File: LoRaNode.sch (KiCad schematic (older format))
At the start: 31 parts, among them J1 Conn_01x09, J2 Conn_01x03, J4 ISP, J5 Conn_01x06, J8 D2, J9 D3, SW1 SW_Push, U1 RFM95W-868S2, U4 ATMEGA328P-AU, Y1 8MHz HC5032/4

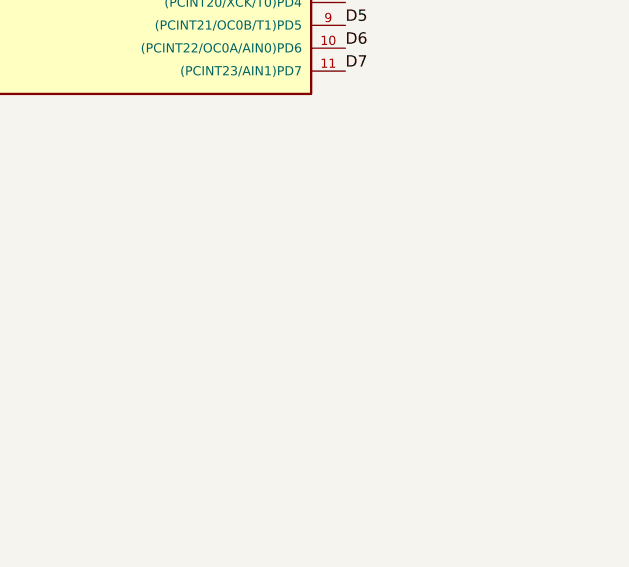
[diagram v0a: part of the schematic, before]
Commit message: Added mounting holes
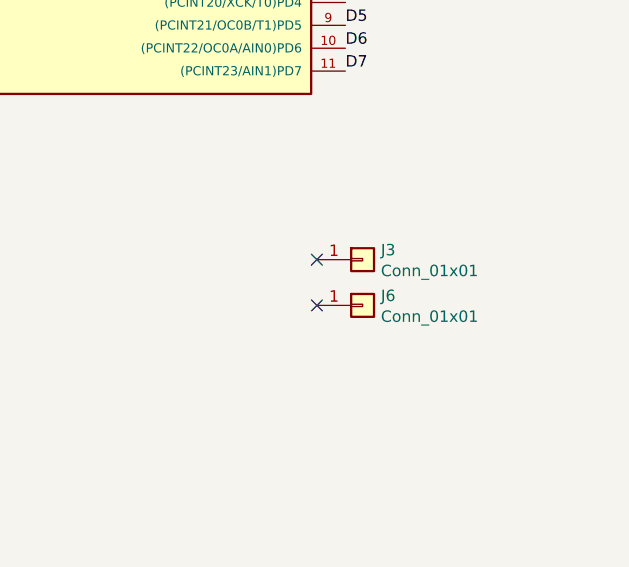
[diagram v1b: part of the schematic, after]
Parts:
- added J3, J6: Conn_01x01, MountingHole:MountingHole_2.2mm_M2, symbol Connector:Conn_01x01
- U1: footprint riske:HOPERF_RFM95W_SMD -> MYLIB:HOPERF_RFM95W_SMD
- U4: footprint Housings_QFP:TQFP-32_7x7mm_Pitch0.8mm -> Package_QFP:TQFP-32_7x7mm_P0.8mm
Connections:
- no-connect marks 3 -> 5
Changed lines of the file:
@@
 F 0 "U1" H 3275 3378 50  0000 C CNN
 F 1 "RFM95W-868S2" H 3625 3150 50  0000 C CNN
-F 2 "riske:HOPERF_RFM95W_SMD" H -25 4350 50  0001 C CNN
+F 2 "MYLIB:HOPERF_RFM95W_SMD" H -25 4350 50  0001 C CNN
 F 3 "" H -25 4350 50  0001 C CNN
 	1    3275 2700
@@
 F 0 "U4" H 7475 4867 50  0000 C CNN
 F 1 "ATMEGA328P-AU" H 7475 4776 50  0000 C CNN
-F 2 "Housings_QFP:TQFP-32_7x7mm_Pitch0.8mm" H 7425 3500 50  0001 C CIN
+F 2 "Package_QFP:TQFP-32_7x7mm_P0.8mm" H 7425 3500 50  0001 C CIN
 F 3 "http://www.atmel.com/images/atmel-8271-8-bit-avr-microcontroller-atmega48a-48pa-88a-88pa-168a-168pa-328-328p_datasheet.pdf" H 7425 3500 50  0001 C CNN
 	1    7425 3500
@@
 Wire Wire Line
 	3475 4500 3600 4500
+$Comp
+L Connector:Conn_01x01 J3
+U 1 1 5CE3EE9D
+P 8500 5525
+F 0 "J3" H 8580 5567 50  0000 L CNN
+F 1 "Conn_01x01" H 8580 5476 50  0000 L CNN
+F 2 "MountingHole:MountingHole_2.2mm_M2" H 8500 5525 50  0001 C CNN
+F 3 "~" H 8500 5525 50  0001 C CNN
+	1    8500 5525
+	1    0    0    -1
+$EndComp
+NoConn ~ 8300 5525
+$Comp
+L Connector:Conn_01x01 J6
+U 1 1 5CE4A02D
+P 8500 5725
+F 0 "J6" H 8580 5767 50  0000 L CNN
+F 1 "Conn_01x01" H 8580 5676 50  0000 L CNN
+F 2 "MountingHole:MountingHole_2.2mm_M2" H 8500 5725 50  0001 C CNN
+F 3 "~" H 8500 5725 50  0001 C CNN
+	1    8500 5725
+	1    0    0    -1
+$EndComp
+NoConn ~ 8300 5725
 $EndSCHEMATC

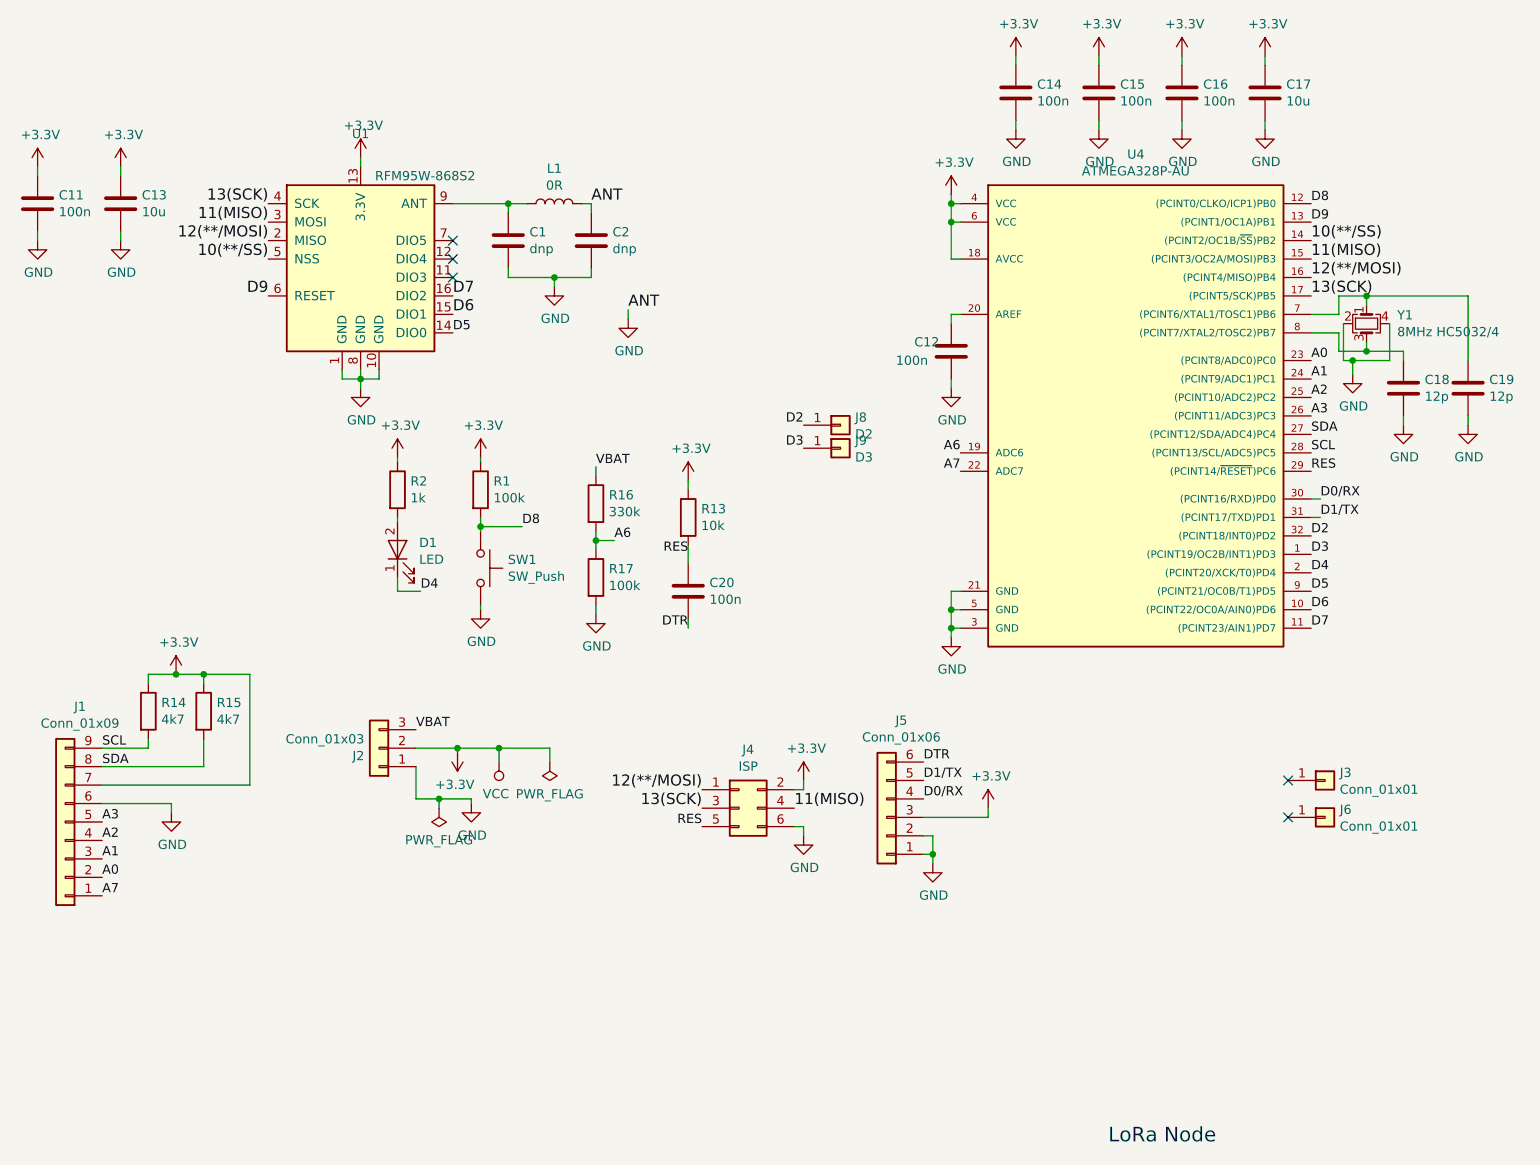
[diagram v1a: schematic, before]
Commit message: Anotation reset, added BOM
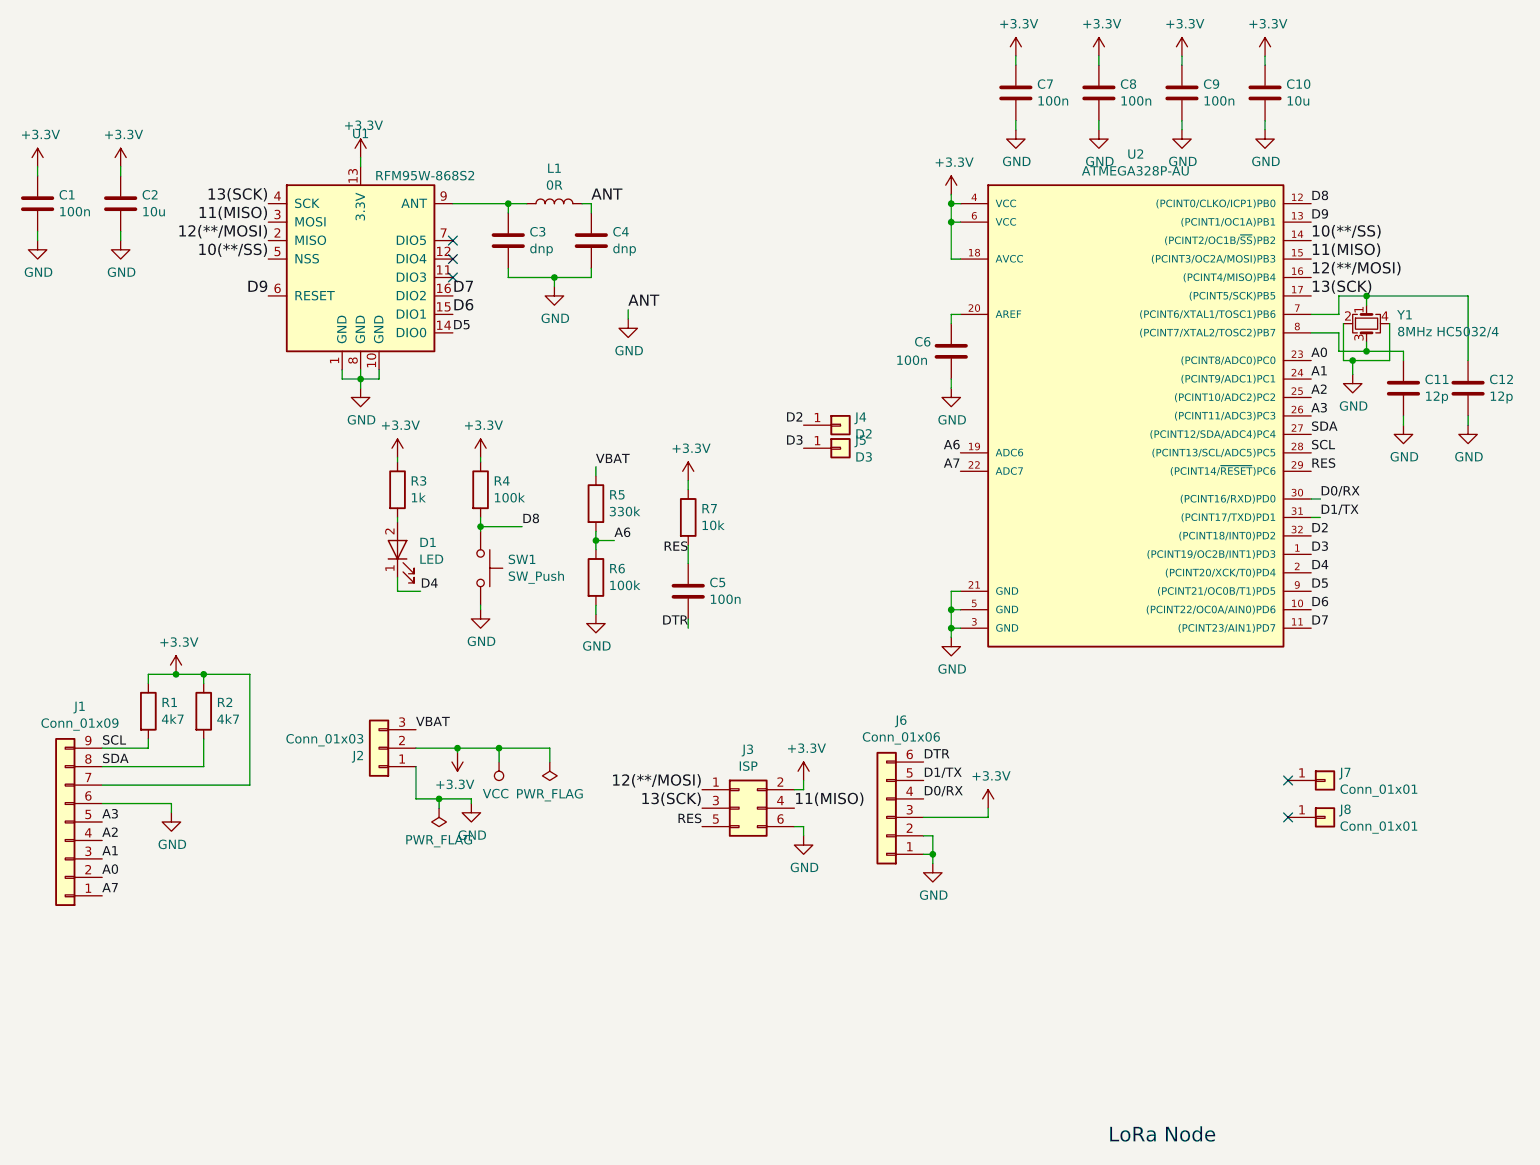
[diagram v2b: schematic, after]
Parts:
- renumbered C11 to C1, C17 to C10, C18 to C11, C19 to C12, C13 to C2, C1 to C3, C2 to C4, C20 to C5, C12 to C6, C14 to C7, C15 to C8, C16 to C9, J4 to J3, J8 to J4, J9 to J5, J5 to J6, J3 to J7, J6 to J8, R14 to R1, R15 to R2, R2 to R3, R1 to R4, R16 to R5, R17 to R6, R13 to R7, U4 to U2
